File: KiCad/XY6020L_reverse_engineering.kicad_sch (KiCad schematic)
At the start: 9 parts, among them Q1 NCE82H140, Q2 NCE82H140, U1 AT32F421KxTx, U2 GS8332SR, U3 GS8332SR, U4 EG1163

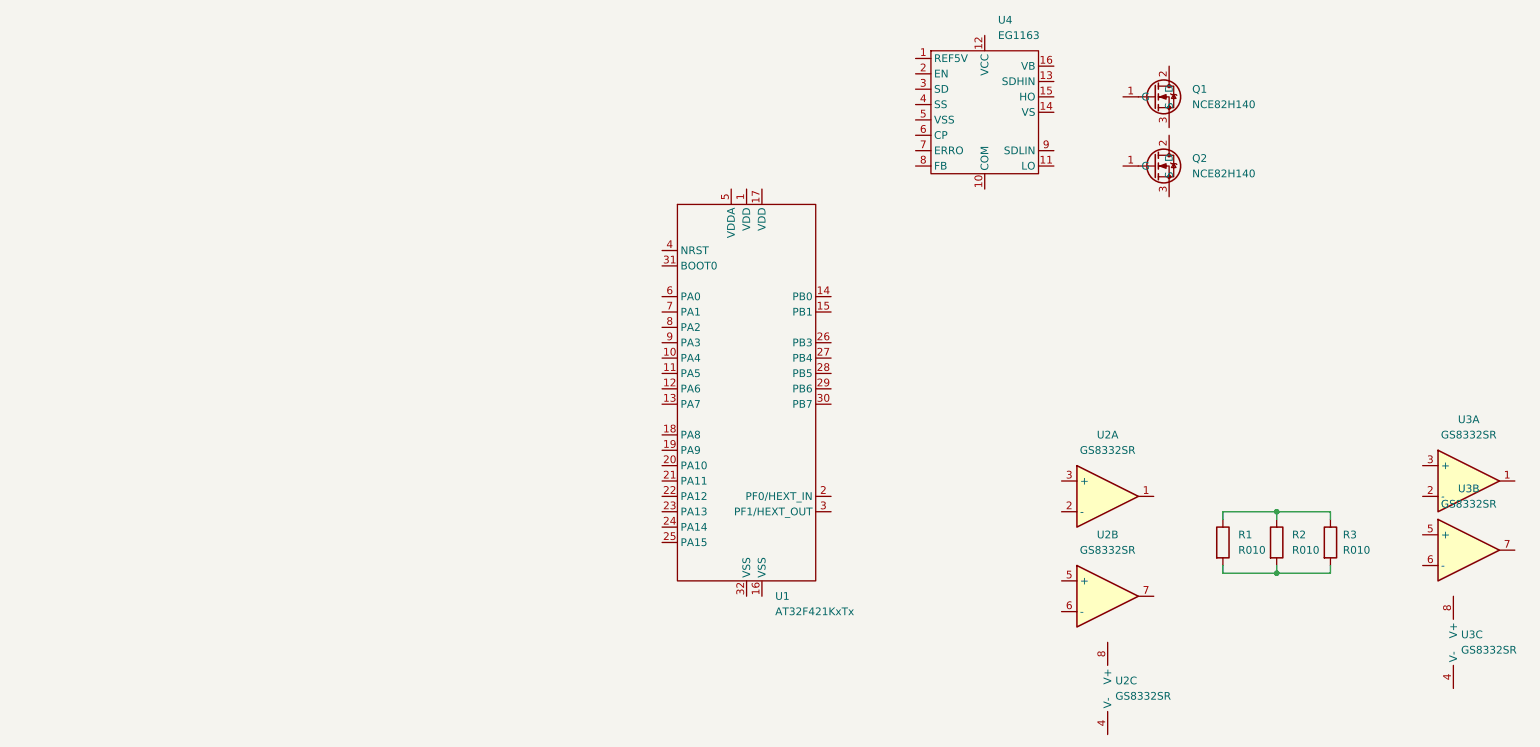
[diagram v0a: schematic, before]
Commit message: Changed reference designators to match the board and started on the op amp circuits. Also separated everything into separate sheets
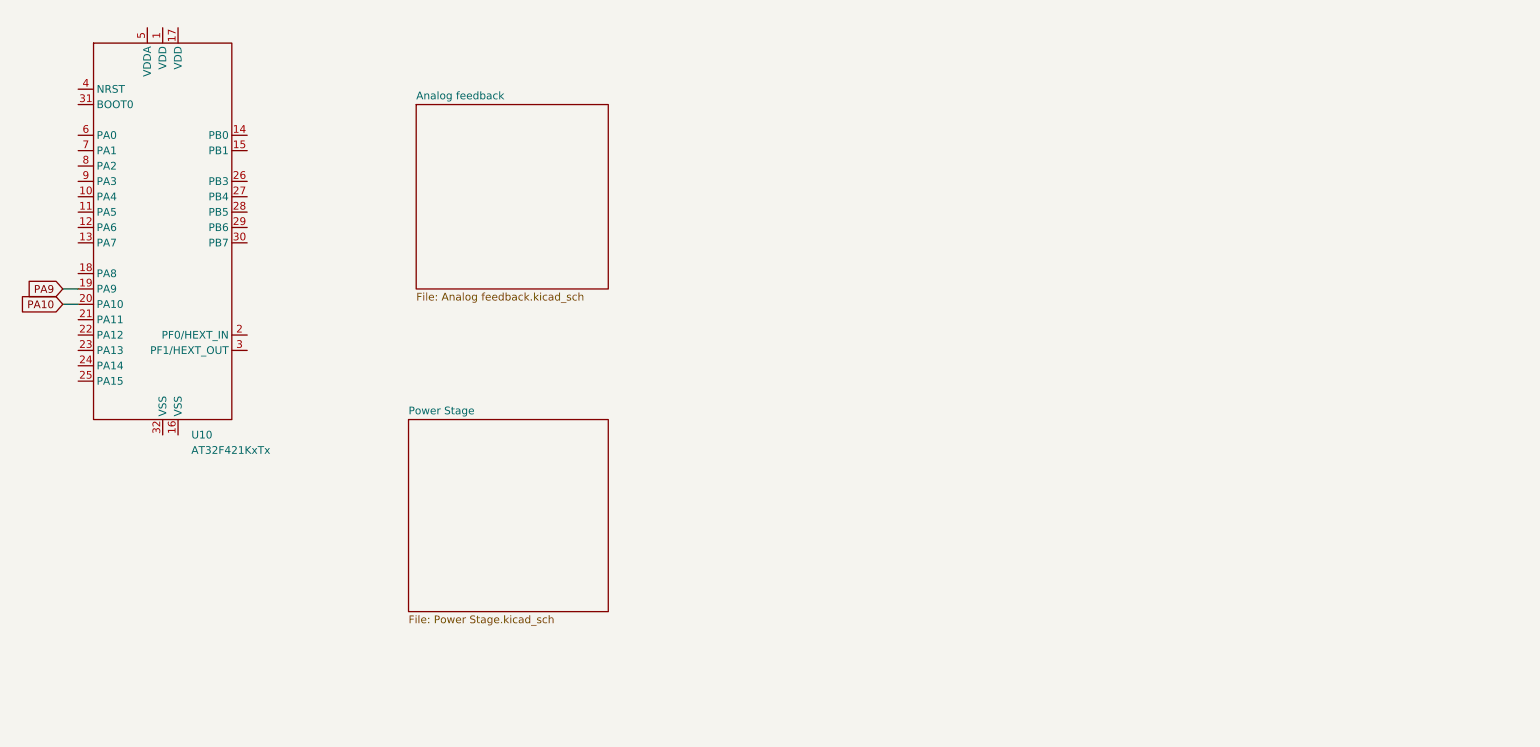
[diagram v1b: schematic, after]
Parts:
- removed Q1, Q2: NCE82H140, Package_TO_SOT_THT:TO-220-3_Vertical, symbol Custom_Transistor_FET:NCE82H140
- removed R1, R2, R3: R010, symbol Device:R
- removed U2, U3: GS8332SR, Package_SO:SOP-8_3.9x4.9mm_P1.27mm, symbol Custom_Amplifier_Operational:GS8332SR
- removed U4: EG1163, Package_SO:SOP-16_3.9x9.9mm_P1.27mm, symbol Custom_Regulator_Switching:EG1163
- renumbered U1 to U10
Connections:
- net PA9: now reaches U10.19 (PA9)
- net PA10: now reaches U10.20 (PA10)
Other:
- added sheet Analog feedback (Analog feedback.kicad_sch)
- added sheet Power Stage (Power Stage.kicad_sch)
- moved on the sheet: U10
